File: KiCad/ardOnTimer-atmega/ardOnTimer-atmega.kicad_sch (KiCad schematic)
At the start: 14 parts, among them K1 KY-019_relay_module, SW1 SW_Push, SW2 SW_Push, SW3 SW_Push, SW4 SW_Push, U3 LCD_HD44780

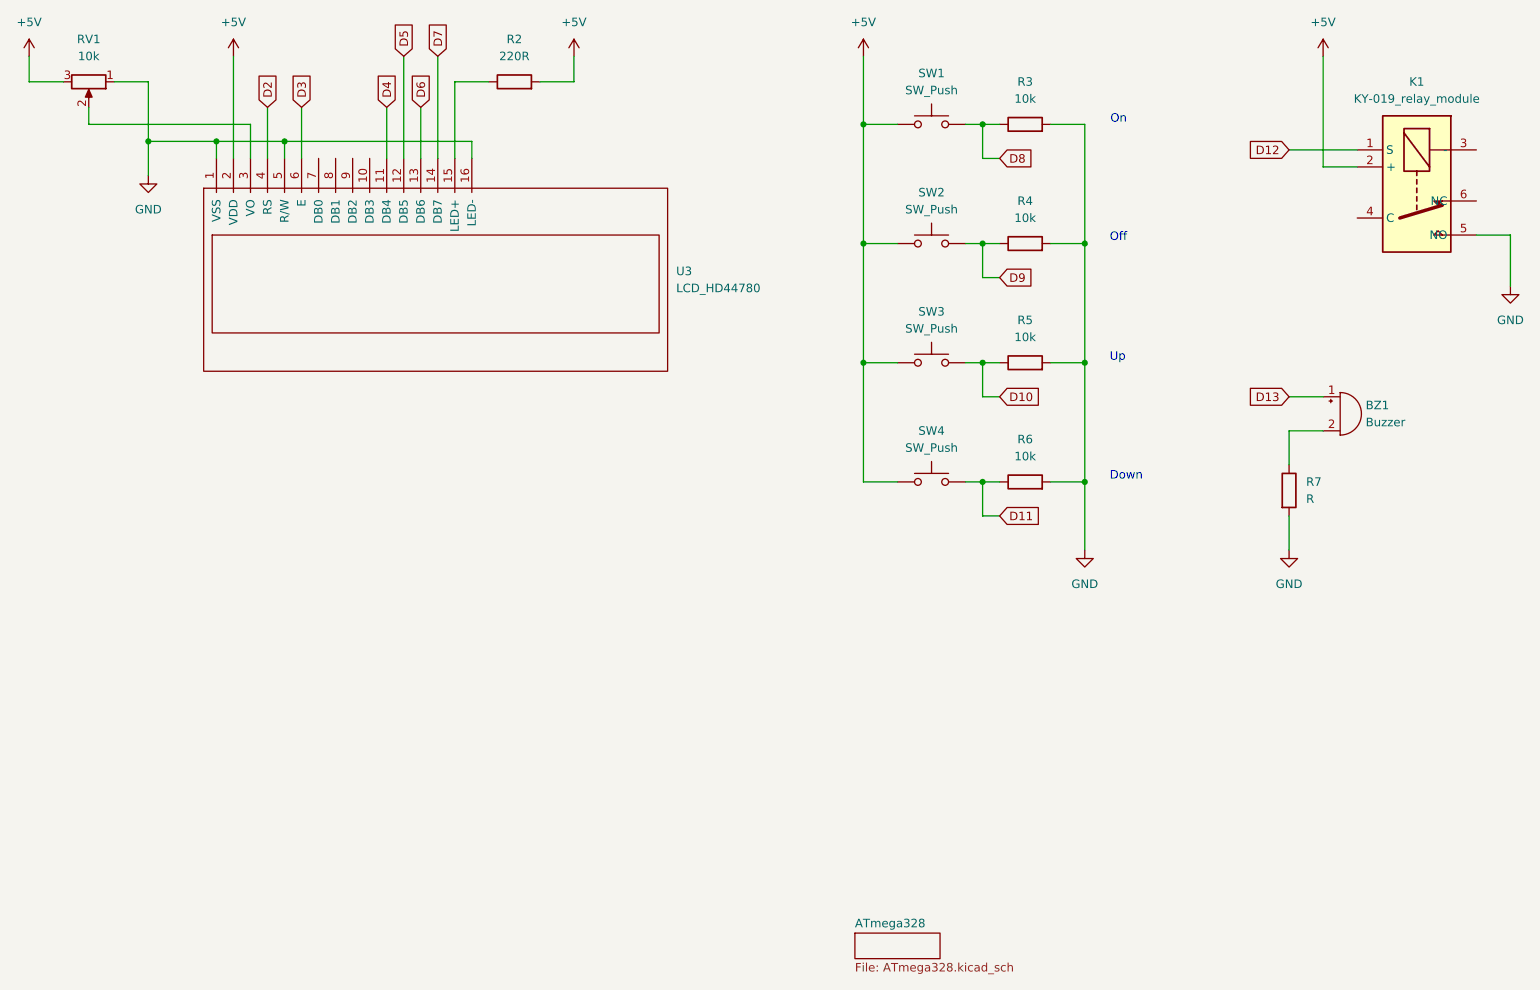
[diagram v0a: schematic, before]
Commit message: 
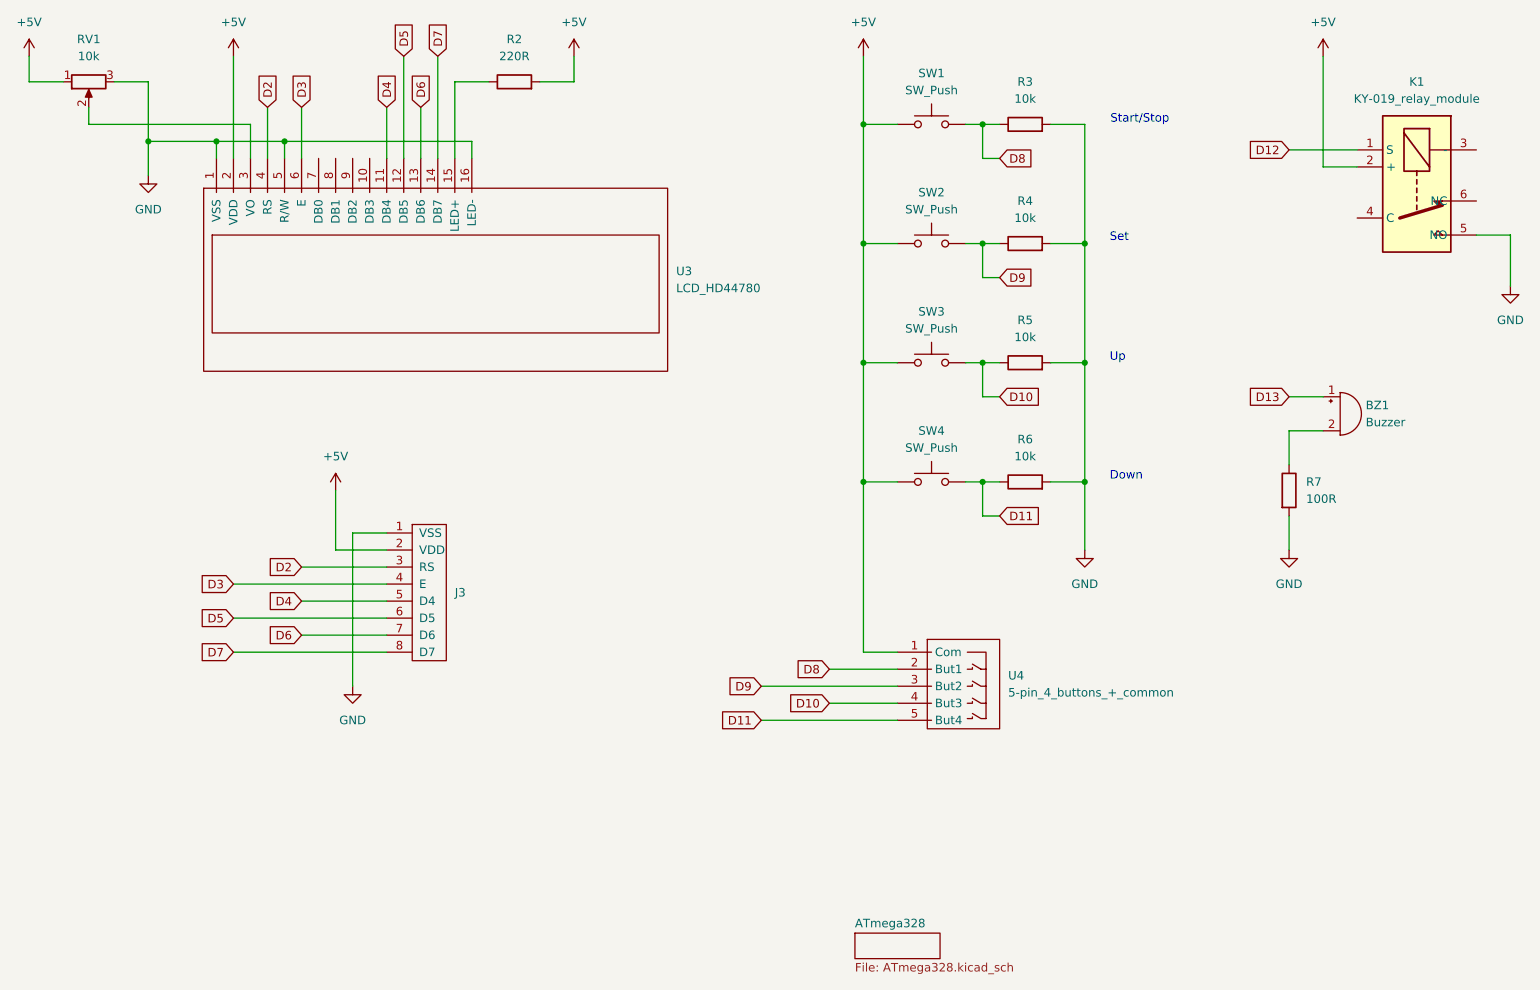
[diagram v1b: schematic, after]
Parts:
- added J3: 8-pin_header_LCD_interface, My_Headers:8-pin JST LCD, symbol My_Headers:8-pin_header_LCD_interface
- added U4: 5-pin_4_buttons_+_common, My_Headers:5-pin JST 4 buttons + common, symbol My_Headers:5-pin_4_buttons_+_common
- R7: value R -> 100R
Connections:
- net +5V: now also RV1.1, J3.2 (VDD), U4.1 (Com); no longer RV1.3
- net D10: now also U4.4 (But3)
- net D11: now also U4.5 (But4)
- net D2: now also J3.3 (RS)
- net D3: now also J3.4 (E)
- net D4: now also J3.5 (D4)
- net D5: now also J3.6 (D5)
- net D6: now also J3.7 (D6)
- net D7: now also J3.8 (D7)
- net D8: now also U4.2 (But1)
- net D9: now also U4.3 (But2)
- net GND: now also RV1.3, J3.1 (VSS); no longer RV1.1
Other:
- note added: "Set"
- note added: "Start/Stop"
- note removed: "Off"
- note removed: "On"
- moved on the sheet: RV1

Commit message: kicad
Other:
- title: (none) -> ardOnTImer-ATmega
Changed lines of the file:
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@@
 (kicad_sch (version 20211123) (generator eeschema)
   (paper "A4")
+  (title_block
+    (title "ardOnTImer-ATmega")
+    (date "2022-09-09")
+    (rev "0.2")
+  )
   (junction (at 162.56 81.28) (diameter 0) (color 0 0 0 0)
   )

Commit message: kicad v0.3
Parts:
- renumbered J3 to J1, R2 to R1, R3 to R2, R4 to R3, R5 to R4, R6 to R5, R7 to R6, U3 to U1, U4 to U2
